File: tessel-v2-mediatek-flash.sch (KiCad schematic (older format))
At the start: 7 parts, among them J401 CONN_01X01, J402 CONN_01X01, U401 S25FL256SAGNFI001

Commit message: 0603 resistor swapped
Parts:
- C401, C402: footprint tm-kicad-lib:SMD-0402 -> tm-kicad-lib:SMD-0402-C
- R401, R402: footprint tm-kicad-lib:SMD-0402 -> tm-kicad-lib:SMD-0402-R
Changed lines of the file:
@@
 LIBS:valves
 LIBS:tm-kicad-lib
+LIBS:nordicsemi
 LIBS:tessel-v2-cache
 EELAYER 25 0
@@
 F 0 "C401" H 7200 5350 40  0000 L CNN
 F 1 "100nF" H 7206 5165 40  0000 L CNN
-F 2 "tm-kicad-lib:SMD-0402" H 7238 5100 30  0001 C CNN
+F 2 "tm-kicad-lib:SMD-0402-C" H 7238 5100 30  0001 C CNN
 F 3 "" H 7200 5250 60  0000 C CNN
 	1    7200 5250
@@
 F 0 "R401" V 6630 5000 40  0000 C CNN
 F 1 "4.7kR" V 6557 5001 40  0000 C CNN
-F 2 "tm-kicad-lib:SMD-0402" V 6480 5000 30  0001 C CNN
+F 2 "tm-kicad-lib:SMD-0402-R" V 6480 5000 30  0001 C CNN
 F 3 "" H 6550 5000 30  0000 C CNN
 	1    6550 5000
@@
 F 0 "R402" V 8930 5000 40  0000 C CNN
 F 1 "4.7kR" V 8857 5001 40  0000 C CNN
-F 2 "tm-kicad-lib:SMD-0402" V 8780 5000 30  0001 C CNN
+F 2 "tm-kicad-lib:SMD-0402-R" V 8780 5000 30  0001 C CNN
 F 3 "" H 8850 5000 30  0000 C CNN
 	1    8850 5000
@@
 F 0 "C402" H 7450 5350 40  0000 L CNN
 F 1 "100nF" H 7456 5165 40  0000 L CNN
-F 2 "tm-kicad-lib:SMD-0402" H 7488 5100 30  0001 C CNN
+F 2 "tm-kicad-lib:SMD-0402-C" H 7488 5100 30  0001 C CNN
 F 3 "" H 7450 5250 60  0000 C CNN
 	1    7450 5250

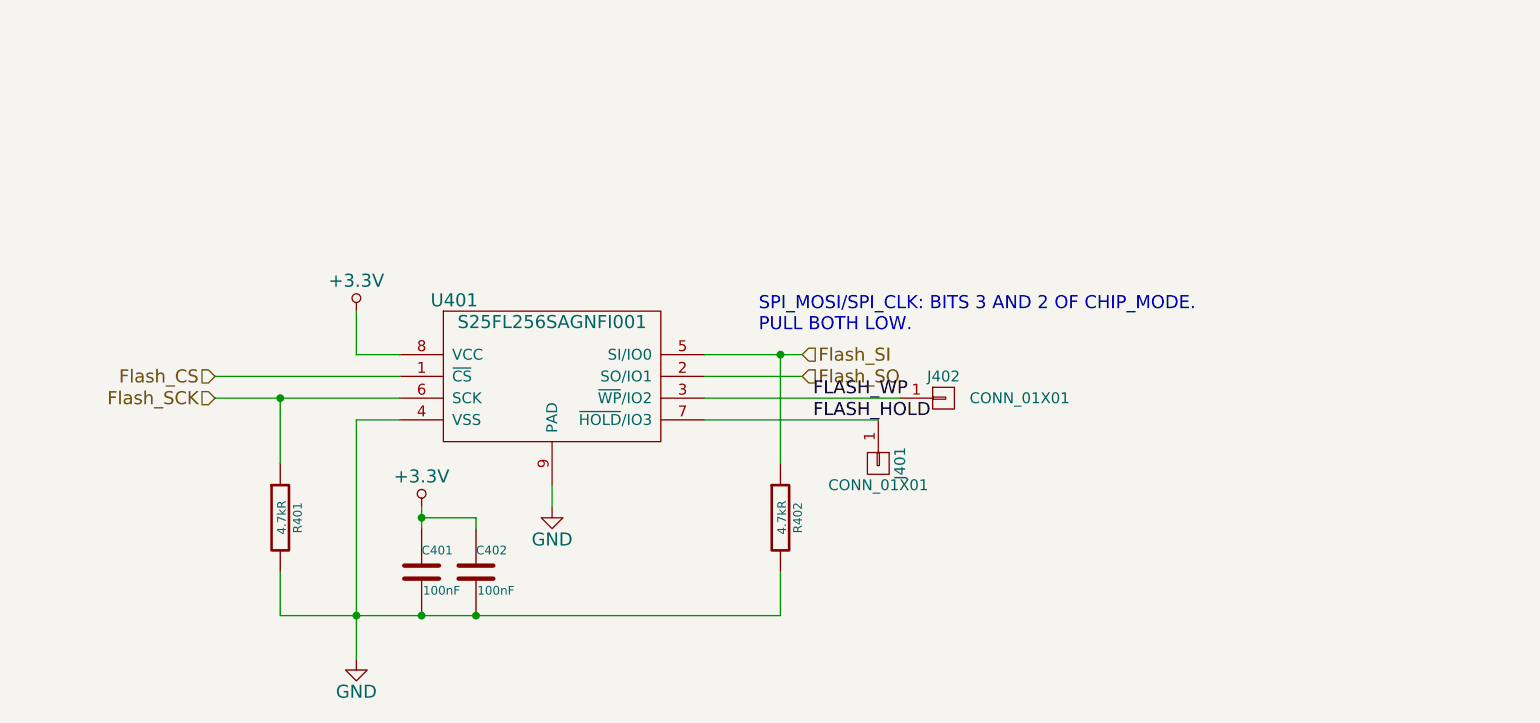
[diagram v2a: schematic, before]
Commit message: most schematic changes done, major refactoring underway
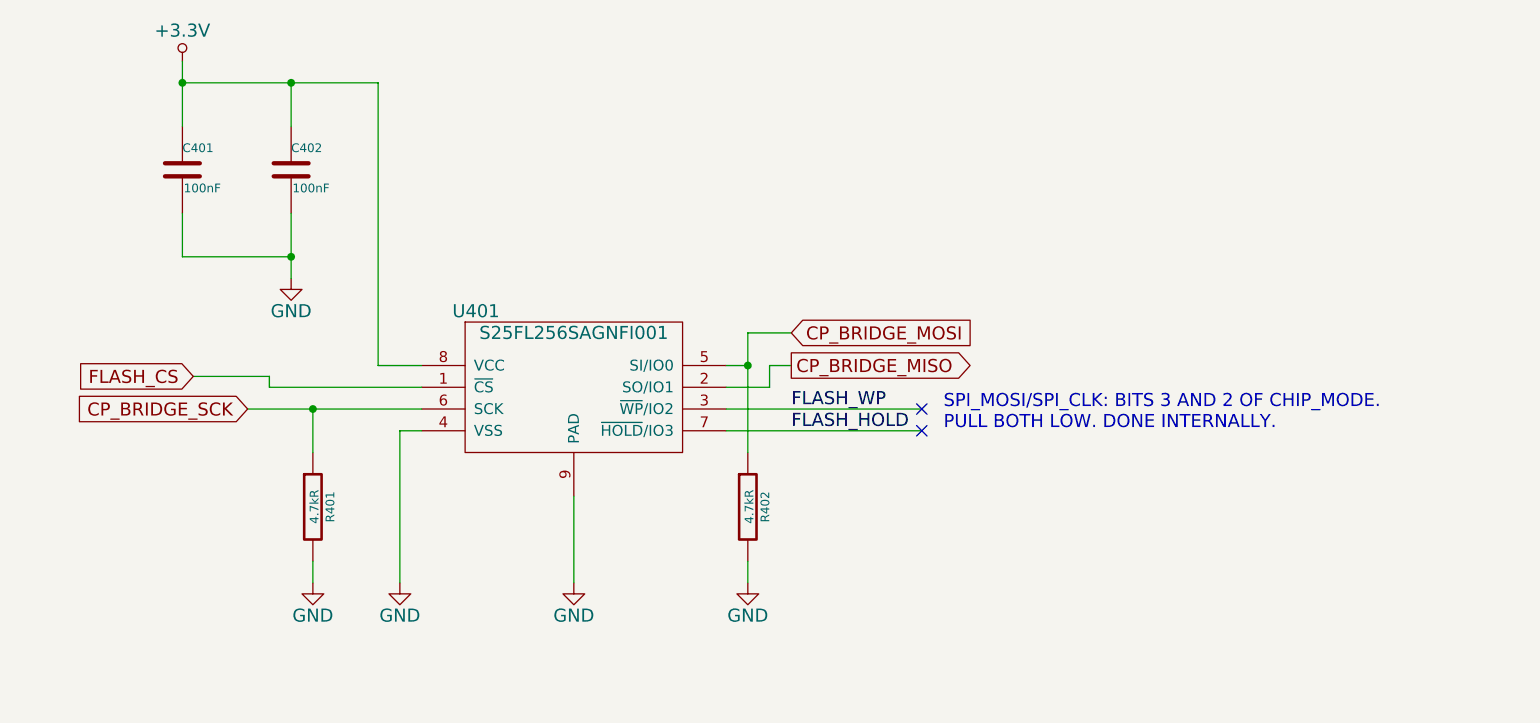
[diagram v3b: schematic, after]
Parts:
- removed J401, J402: CONN_01X01, tm-kicad-lib:Testpoint, symbol CONN_01X01
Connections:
- net Flash_CS renamed FLASH_CS
- net Flash_SCK renamed CP_BRIDGE_SCK
- net Flash_SI renamed CP_BRIDGE_MOSI
- net Flash_SO renamed CP_BRIDGE_MISO
- no-connect marks 0 -> 2
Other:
- note added: "SPI_MOSI/SPI_CLK: BITS 3 AND 2 OF CHIP_MODE.\nPULL BOTH LOW. DONE INTERNALLY."
- note removed: "SPI_MOSI/SPI_CLK: BITS 3 AND 2 OF CHIP_MODE.\nPULL BOTH LOW."
- moved on the sheet: C401, C402, R401, R402, U401

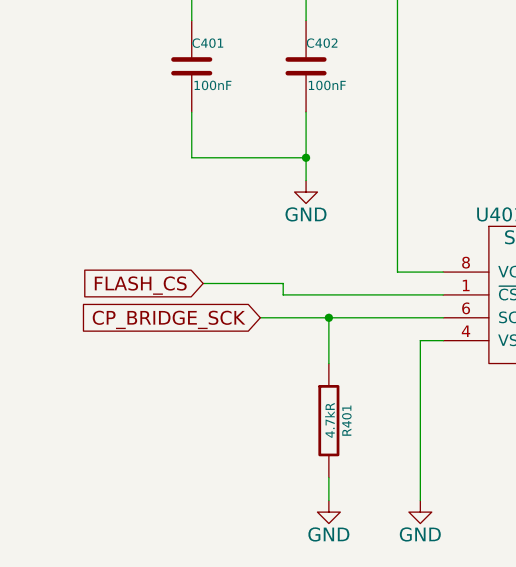
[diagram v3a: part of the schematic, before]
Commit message: still refactoring. usb is a pain
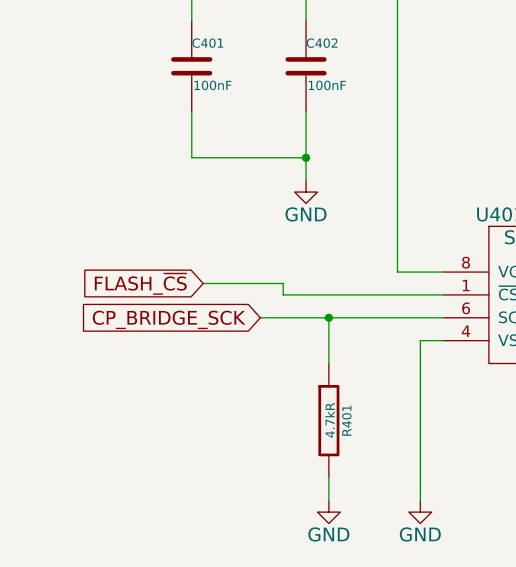
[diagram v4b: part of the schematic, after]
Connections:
- net FLASH_CS renamed FLASH_~CS
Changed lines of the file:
@@
 Connection ~ 6600 3000
 Text GLabel 6150 4350 0    60   Input ~ 0
-FLASH_CS
+FLASH_~CS
 $EndSCHEMATC

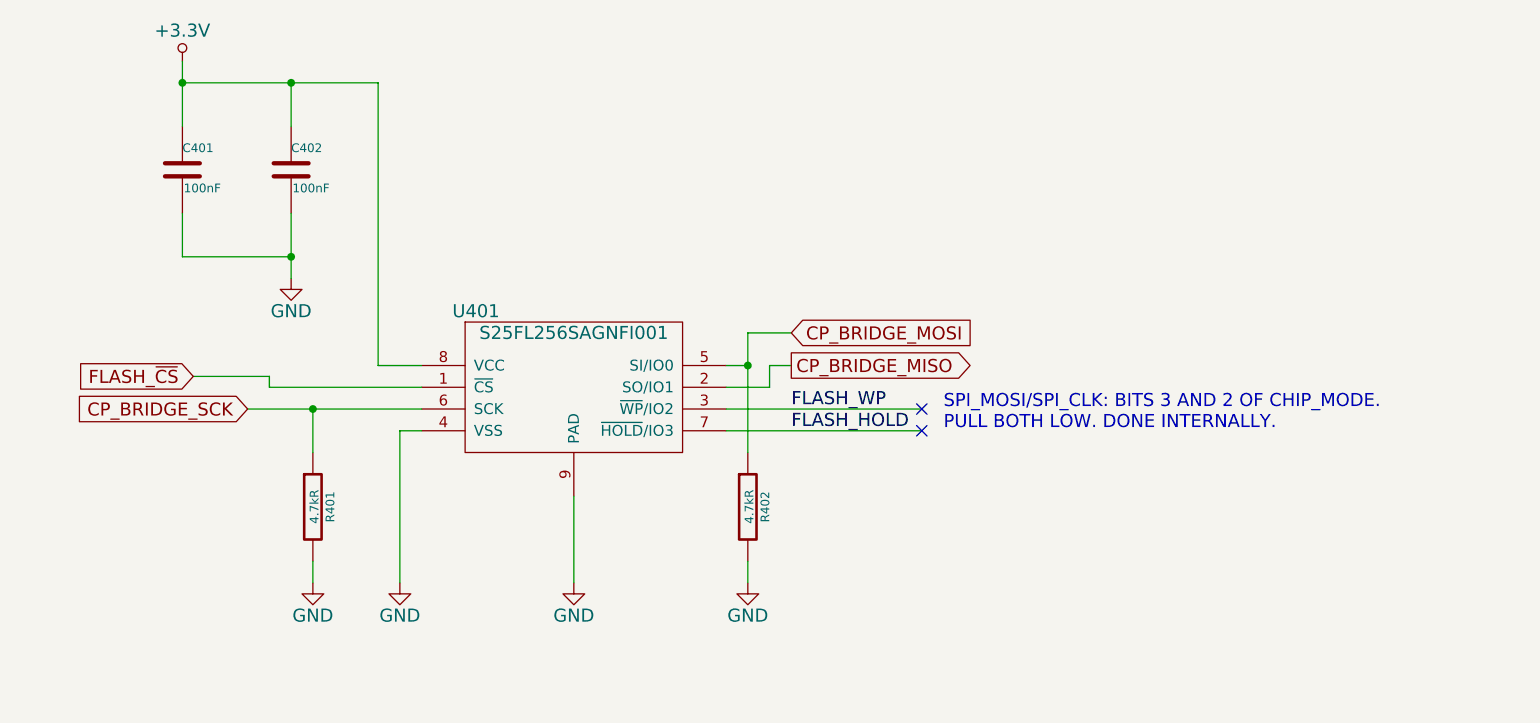
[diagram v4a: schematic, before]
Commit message: reset annotation
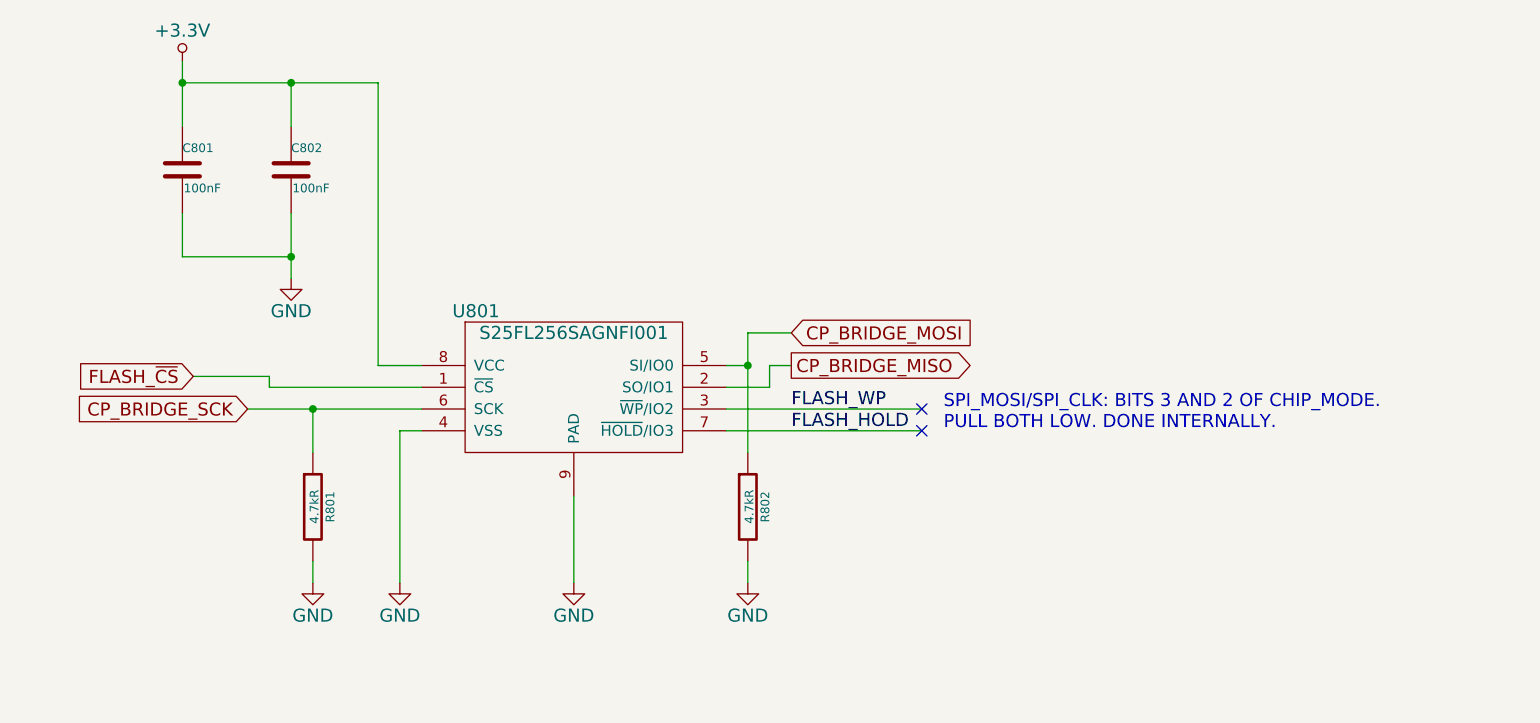
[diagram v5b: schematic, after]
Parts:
- renumbered C401 to C801, C402 to C802, R401 to R801, R402 to R802, U401 to U801
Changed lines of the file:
@@
 $EndDescr
 $Comp
-L S25FL256SAGNFI001 U401
+L S25FL256SAGNFI001 U801
 U 1 1 548FCC1A
 P 7900 4400
-AR Path="/548C90C9/548CC15A/548FCC1A" Ref="U401"  Part="1"
-AR Path="/548CC15A/548FCC1A" Ref="U401"  Part="1"
-F 0 "U401" H 7450 4750 60  0000 C CNN
+F 0 "U801" H 7450 4750 60  0000 C CNN
 F 1 "S25FL256SAGNFI001" H 7900 4650 60  0000 C CNN
 F 2 "tm-kicad-lib:WNG008" H 7500 5400 60  0001 C CNN
@@
 $EndComp
 $Comp
-L GND #PWR029
+L GND #PWR804
 U 1 1 548FCCD4
 P 7100 5300
-AR Path="/548C90C9/548CC15A/548FCCD4" Ref="#PWR029"  Part="1"
-AR Path="/548CC15A/548FCCD4" Ref="#PWR029"  Part="1"
-F 0 "#PWR029" H 7100 5050 60  0001 C CNN
+F 0 "#PWR804" H 7100 5050 60  0001 C CNN
 F 1 "GND" H 7100 5150 60  0000 C CNN
 F 2 "" H 7100 5300 60  0000 C CNN
@@
 $EndComp
 $Comp
-L C C401
+L C C801
 U 1 1 548FCD34
 P 6100 3400
-AR Path="/548C90C9/548CC15A/548FCD34" Ref="C401"  Part="1"
-AR Path="/548CC15A/548FCD34" Ref="C401"  Part="1"
-F 0 "C401" H 6100 3500 40  0000 L CNN
+F 0 "C801" H 6100 3500 40  0000 L CNN
 F 1 "100nF" H 6106 3315 40  0000 L CNN
 F 2 "tm-kicad-lib:SMD-0402-C" H 6138 3250 30  0001 C CNN
@@
 $EndComp
 $Comp
-L +3.3V #PWR031
+L +3.3V #PWR801
 U 1 1 548FCD90
 P 6100 2900
-AR Path="/548C90C9/548CC15A/548FCD90" Ref="#PWR031"  Part="1"
-AR Path="/548CC15A/548FCD90" Ref="#PWR031"  Part="1"
-F 0 "#PWR031" H 6100 2750 60  0001 C CNN
+F 0 "#PWR801" H 6100 2750 60  0001 C CNN
 F 1 "+3.3V" H 6100 3040 60  0000 C CNN
 F 2 "" H 6100 2900 60  0000 C CNN
@@
 SPI_MOSI/SPI_CLK: BITS 3 AND 2 OF CHIP_MODE.\nPULL BOTH LOW. DONE INTERNALLY.
 $Comp
-L R R401
+L R R801
 U 1 1 549239D5
 P 6700 4950
-AR Path="/548C90C9/548CC15A/549239D5" Ref="R401"  Part="1"
-AR Path="/548CC15A/549239D5" Ref="R401"  Part="1"
-F 0 "R401" V 6780 4950 40  0000 C CNN
+F 0 "R801" V 6780 4950 40  0000 C CNN
 F 1 "4.7kR" V 6707 4951 40  0000 C CNN
 F 2 "tm-kicad-lib:SMD-0402-R" V 6630 4950 30  0001 C CNN
@@
 	6700 5200 6700 5300
 $Comp
-L R R402
+L R R802
 U 1 1 54923AA1
 P 8700 4950
-AR Path="/548C90C9/548CC15A/54923AA1" Ref="R402"  Part="1"
-AR Path="/548CC15A/54923AA1" Ref="R402"  Part="1"
-F 0 "R402" V 8780 4950 40  0000 C CNN
+F 0 "R802" V 8780 4950 40  0000 C CNN
 F 1 "4.7kR" V 8707 4951 40  0000 C CNN
 F 2 "tm-kicad-lib:SMD-0402-R" V 8630 4950 30  0001 C CNN
@@
 	8600 4500 9500 4500
 $Comp
-L GND #PWR032
+L GND #PWR805
 U 1 1 5495E6FE
 P 7900 5300
-AR Path="/548C90C9/548CC15A/5495E6FE" Ref="#PWR032"  Part="1"
-AR Path="/548CC15A/5495E6FE" Ref="#PWR032"  Part="1"
-F 0 "#PWR032" H 7900 5050 60  0001 C CNN
+F 0 "#PWR805" H 7900 5050 60  0001 C CNN
 F 1 "GND" H 7900 5150 60  0000 C CNN
 F 2 "" H 7900 5300 60  0000 C CNN
@@
 FLASH_WP
 $Comp
-L C C402
+L C C802
 U 1 1 54C991E6
 P 6600 3400
-AR Path="/548C90C9/548CC15A/54C991E6" Ref="C402"  Part="1"
-AR Path="/548CC15A/54C991E6" Ref="C402"  Part="1"
-F 0 "C402" H 6600 3500 40  0000 L CNN
+F 0 "C802" H 6600 3500 40  0000 L CNN
 F 1 "100nF" H 6606 3315 40  0000 L CNN
 F 2 "tm-kicad-lib:SMD-0402-C" H 6638 3250 30  0001 C CNN
@@
 	7100 4600 7100 5300
 $Comp
-L GND #PWR?
+L GND #PWR806
 U 1 1 54EAD50E
 P 8700 5300
-AR Path="/548C90C9/548CC15A/54EAD50E" Ref="#PWR?"  Part="1"
-AR Path="/548CC15A/54EAD50E" Ref="#PWR?"  Part="1"
-F 0 "#PWR?" H 8700 5050 60  0001 C CNN
+F 0 "#PWR806" H 8700 5050 60  0001 C CNN
 F 1 "GND" H 8700 5150 60  0000 C CNN
 F 2 "" H 8700 5300 60  0000 C CNN
@@
 $EndComp
 $Comp
-L GND #PWR?
+L GND #PWR803
 U 1 1 54EAD519
 P 6700 5300
-AR Path="/548C90C9/548CC15A/54EAD519" Ref="#PWR?"  Part="1"
-AR Path="/548CC15A/54EAD519" Ref="#PWR?"  Part="1"
-F 0 "#PWR?" H 6700 5050 60  0001 C CNN
+F 0 "#PWR803" H 6700 5050 60  0001 C CNN
 F 1 "GND" H 6700 5150 60  0000 C CNN
 F 2 "" H 6700 5300 60  0000 C CNN
@@
 	6600 3800 6600 3900
 $Comp
-L GND #PWR?
+L GND #PWR802
 U 1 1 54EAF476
 P 6600 3900
-AR Path="/548C90C9/548CC15A/54EAF476" Ref="#PWR?"  Part="1"
-AR Path="/548CC15A/54EAF476" Ref="#PWR?"  Part="1"
-F 0 "#PWR?" H 6600 3650 60  0001 C CNN
+F 0 "#PWR802" H 6600 3650 60  0001 C CNN
 F 1 "GND" H 6600 3750 60  0000 C CNN
 F 2 "" H 6600 3900 60  0000 C CNN

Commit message: annotation did not take?
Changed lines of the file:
@@
 	7200 4400 6500 4400
 Wire Wire Line
-	6400 4500 6700 4500
-Wire Wire Line
-	6700 4500 7200 4500
+	6400 4500 7200 4500
 Wire Wire Line
 	8600 4300 8700 4300
@@
 	7000 3000 7000 4300
 Wire Wire Line
-	6100 2900 6100 3000
-Wire Wire Line
-	6100 3000 6100 3200
+	6100 2900 6100 3200
 Wire Wire Line
 	6700 4700 6700 4500
@@
 $EndComp
 Wire Wire Line
-	8700 4150 8700 4300
-Wire Wire Line
-	8700 4300 8700 4700
+	8700 4150 8700 4700
 Connection ~ 8700 4300
 Wire Wire Line
@@
 	6600 3200 6600 3000
 Wire Wire Line
-	6100 3000 6600 3000
-Wire Wire Line
-	6600 3000 7000 3000
+	6100 3000 7000 3000
 Connection ~ 6100 3000
 Text GLabel 8900 4150 2    60   Input ~ 0
@@
 	6100 3800 6600 3800
 Wire Wire Line
-	6600 3600 6600 3800
-Wire Wire Line
-	6600 3800 6600 3900
+	6600 3600 6600 3900
 $Comp
 L GND #PWR802
